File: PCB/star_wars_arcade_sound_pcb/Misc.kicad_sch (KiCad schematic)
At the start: 14 parts, among them P1 sw_main_connector, P2 sw_aud_connector, P3 sw_audio_edge_connector

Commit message: Began PCB layout
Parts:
- P1: footprint (none) -> atari:P1
- P2: footprint (none) -> atari:Aud_Con
- P3: footprint (none) -> atari:P3
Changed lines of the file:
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@@
       (effects (font (size 1.27 1.27)) (justify left))
     )
-    (property "Footprint" "" (id 2) (at 103.505 99.06 0)
+    (property "Footprint" "atari:Aud_Con" (id 2) (at 103.505 99.06 0)
       (effects (font (size 1.27 1.27)) hide)
     )
@@
     (property "Reference" "P3" (id 0) (at 114.6175 32.9905 0))
     (property "Value" "sw_audio_edge_connector" (id 1) (at 114.935 34.925 0))
-    (property "Footprint" "" (id 2) (at 112.395 53.34 0)
+    (property "Footprint" "atari:P3" (id 2) (at 112.395 53.34 0)
       (effects (font (size 1.27 1.27)) hide)
     )
@@
     (property "Reference" "P1" (id 0) (at 48.5775 30.4505 0))
     (property "Value" "sw_main_connector" (id 1) (at 48.895 32.385 0))
-    (property "Footprint" "" (id 2) (at 48.26 86.36 0)
-      (effects (font (size 1.27 1.27)) hide)
-    )
+    (property "Footprint" "atari:P1" (id 2) (at 48.26 86.36 0)
+      (effects (font (size 1.27 1.27)) hide)
+    )

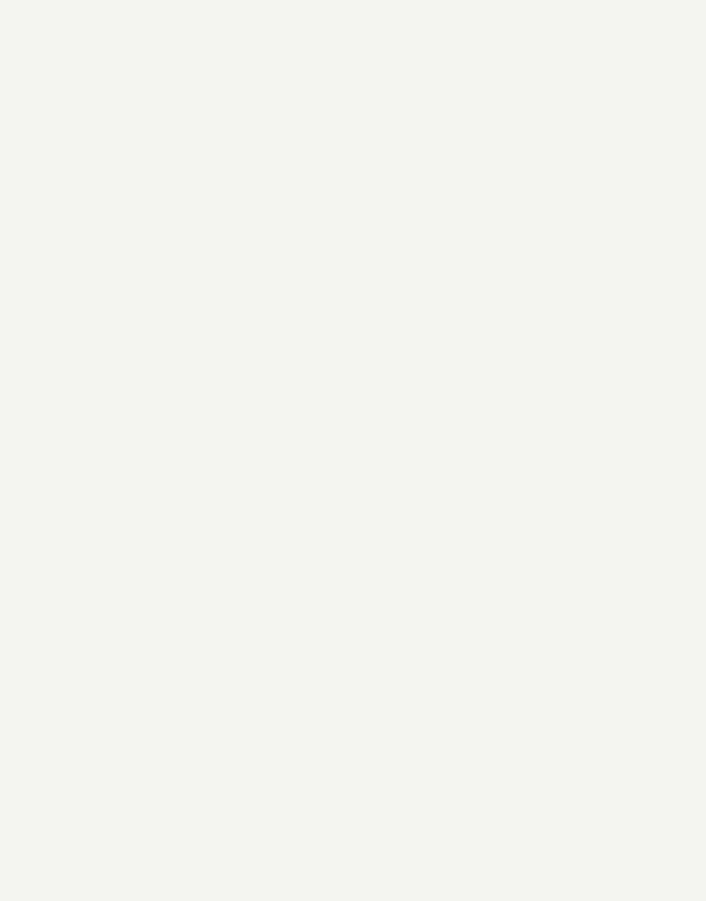
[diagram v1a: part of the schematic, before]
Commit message: Placed all components
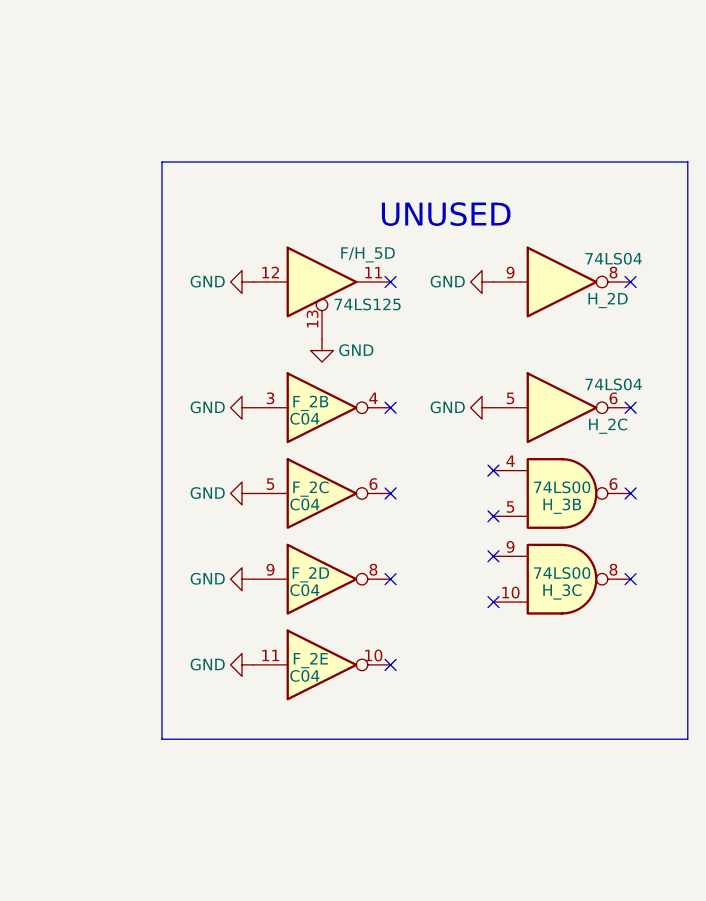
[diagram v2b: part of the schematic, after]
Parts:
- added F/H_5: 74LS125, atari:DIP14, symbol atari:74LS125
- added F_2: C04, atari:DIP14, symbol atari:74LS05
- added H_2: 74LS04, atari:DIP14, symbol atari:74LS04
- added H_3: 74LS00, atari:DIP14, symbol atari:74LS00
- C13, C15: footprint (none) -> atari:LargeCap1
- C14: footprint (none) -> atari:LargeCap2
- DS1: footprint (none) -> atari:LED
- R7: footprint (none) -> atari:GenericComp
- TP11, TP12, TP3, TP4, TP5, TP6: footprint (none) -> atari:TEST_POINT
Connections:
- net GND: now also F/H_5.12, F/H_5.13, F_2.11, F_2.3, F_2.5, F_2.9, H_2.5, H_2.9
- no-connect marks 48 -> 61
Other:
- note added: "UNUSED"
